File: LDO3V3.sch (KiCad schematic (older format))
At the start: 3 parts, among them U9 TPS727

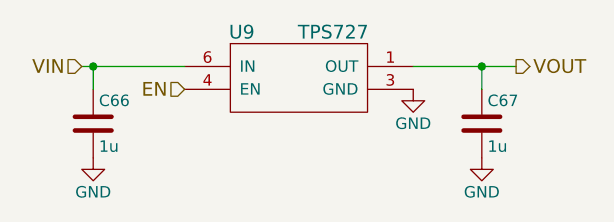
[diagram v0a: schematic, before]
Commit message: Added barrel jack and ideal diode circuit
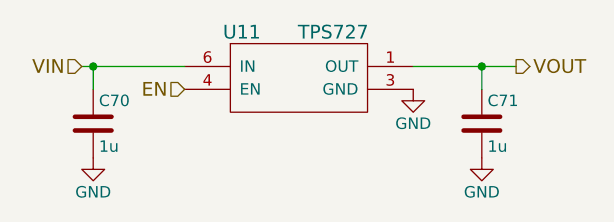
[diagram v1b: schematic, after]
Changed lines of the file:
@@
 AR Path="/55C83E6D/55C7E073" Ref="U10"  Part="1"
 AR Path="/55C84A5F/55C7E073" Ref="U11"  Part="1"
-F 0 "U9" H 2850 2100 60  0000 C CNN
+F 0 "U11" H 2850 2100 60  0000 C CNN
 F 1 "TPS727" H 3250 2100 60  0000 C CNN
 F 2 "SMD_Packages:S-PWSON-N6" H 3100 1900 60  0001 C CNN
@@
 AR Path="/55C83E6D/55C7E0BA" Ref="C68"  Part="1"
 AR Path="/55C84A5F/55C7E0BA" Ref="C70"  Part="1"
-F 0 "C66" H 2225 2200 50  0000 L CNN
+F 0 "C70" H 2225 2200 50  0000 L CNN
 F 1 "1u" H 2225 2000 50  0000 L CNN
 F 2 "Capacitors_SMD:C_0603" H 2238 1950 30  0001 C CNN
@@
 AR Path="/55C83E6D/55C7E105" Ref="C69"  Part="1"
 AR Path="/55C84A5F/55C7E105" Ref="C71"  Part="1"
-F 0 "C67" H 3925 2200 50  0000 L CNN
+F 0 "C71" H 3925 2200 50  0000 L CNN
 F 1 "1u" H 3925 2000 50  0000 L CNN
 F 2 "Capacitors_SMD:C_0603" H 3938 1950 30  0001 C CNN
@@
 $EndComp
 $Comp
-L GND #PWR097
+L GND #PWR0108
 U 1 1 55C7E1D1
 P 3600 1950
-AR Path="/55C7CD38/55C7E1D1" Ref="#PWR097"  Part="1"
-AR Path="/55C83E6D/55C7E1D1" Ref="#PWR0100"  Part="1"
-AR Path="/55C84A5F/55C7E1D1" Ref="#PWR0103"  Part="1"
-F 0 "#PWR0103" H 3600 1700 50  0001 C CNN
+AR Path="/55C7CD38/55C7E1D1" Ref="#PWR0108"  Part="1"
+AR Path="/55C83E6D/55C7E1D1" Ref="#PWR0111"  Part="1"
+AR Path="/55C84A5F/55C7E1D1" Ref="#PWR0114"  Part="1"
+F 0 "#PWR0114" H 3600 1700 50  0001 C CNN
 F 1 "GND" H 3600 1800 50  0000 C CNN
 F 2 "" H 3600 1950 60  0000 C CNN
@@
 $EndComp
 $Comp
-L GND #PWR098
+L GND #PWR0109
 U 1 1 55C7E1EC
 P 3900 2250
-AR Path="/55C7CD38/55C7E1EC" Ref="#PWR098"  Part="1"
-AR Path="/55C83E6D/55C7E1EC" Ref="#PWR0101"  Part="1"
-AR Path="/55C84A5F/55C7E1EC" Ref="#PWR0104"  Part="1"
-F 0 "#PWR0104" H 3900 2000 50  0001 C CNN
+AR Path="/55C7CD38/55C7E1EC" Ref="#PWR0109"  Part="1"
+AR Path="/55C83E6D/55C7E1EC" Ref="#PWR0112"  Part="1"
+AR Path="/55C84A5F/55C7E1EC" Ref="#PWR0115"  Part="1"
+F 0 "#PWR0115" H 3900 2000 50  0001 C CNN
 F 1 "GND" H 3900 2100 50  0000 C CNN
 F 2 "" H 3900 2250 60  0000 C CNN
@@
 $EndComp
 $Comp
-L GND #PWR099
+L GND #PWR0110
 U 1 1 55C7E200
 P 2200 2250
-AR Path="/55C7CD38/55C7E200" Ref="#PWR099"  Part="1"
-AR Path="/55C83E6D/55C7E200" Ref="#PWR0102"  Part="1"
-AR Path="/55C84A5F/55C7E200" Ref="#PWR0105"  Part="1"
-F 0 "#PWR0105" H 2200 2000 50  0001 C CNN
+AR Path="/55C7CD38/55C7E200" Ref="#PWR0110"  Part="1"
+AR Path="/55C83E6D/55C7E200" Ref="#PWR0113"  Part="1"
+AR Path="/55C84A5F/55C7E200" Ref="#PWR0116"  Part="1"
+F 0 "#PWR0116" H 2200 2000 50  0001 C CNN
 F 1 "GND" H 2200 2100 50  0000 C CNN
 F 2 "" H 2200 2250 60  0000 C CNN
